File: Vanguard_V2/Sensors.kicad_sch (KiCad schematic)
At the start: 20 parts, among them IC2 MAX-M10S-00B, IC3 ADXL375BCCZ-RL, IC4 ASM330LHHTR, J7 Conn_Coaxial, U4 LPS22HH, U5 LSM303C

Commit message: V2 Board Ready
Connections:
- net +3.3V: now also C24.1, C25.1, C26.1, IC4.5 (VDDIO)
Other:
- moved on the sheet: C21, C22, C23, C24, C27, C28, C29, C30, D3, FB2, IC2, IC3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

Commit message: started layout for V2.1
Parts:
- R11: footprint Capacitor_SMD:C_0402_1005Metric -> Resistor_SMD:R_0402_1005Metric
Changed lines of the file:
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@@
 			)
 		)
-		(property "Footprint" "Capacitor_SMD:C_0402_1005Metric"
+		(property "Footprint" "Resistor_SMD:R_0402_1005Metric"
 			(at 196.85 126.238 90)
 			(effects

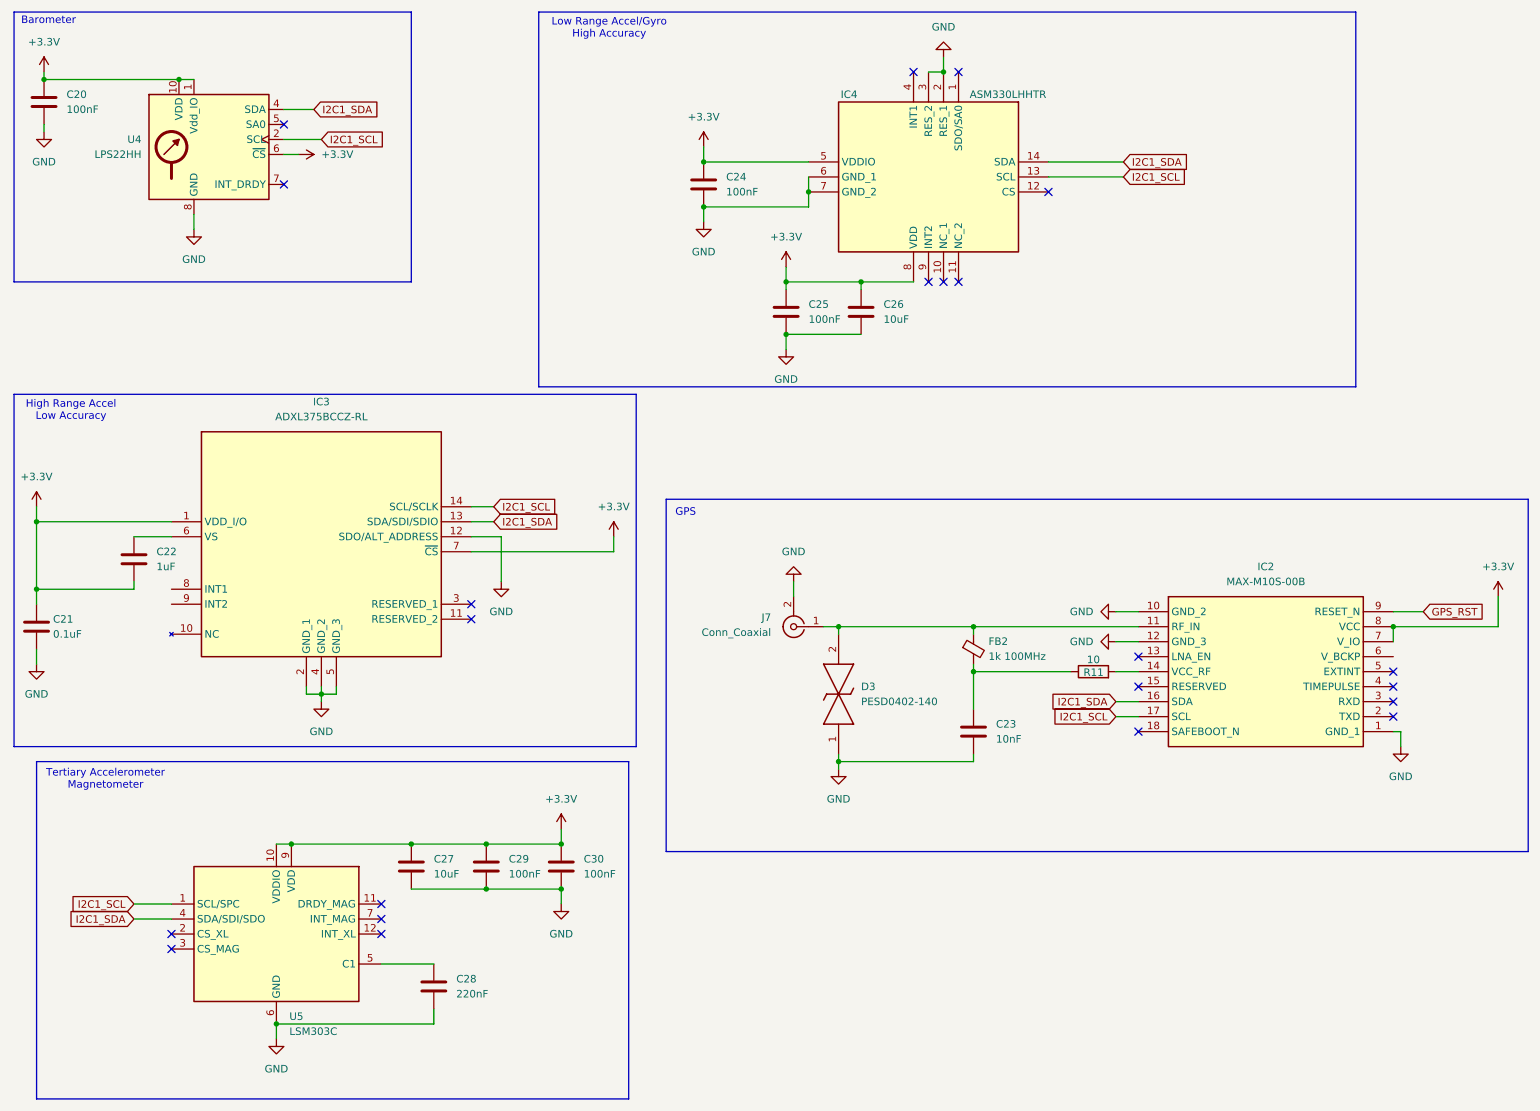
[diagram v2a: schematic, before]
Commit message: Fixed sensors
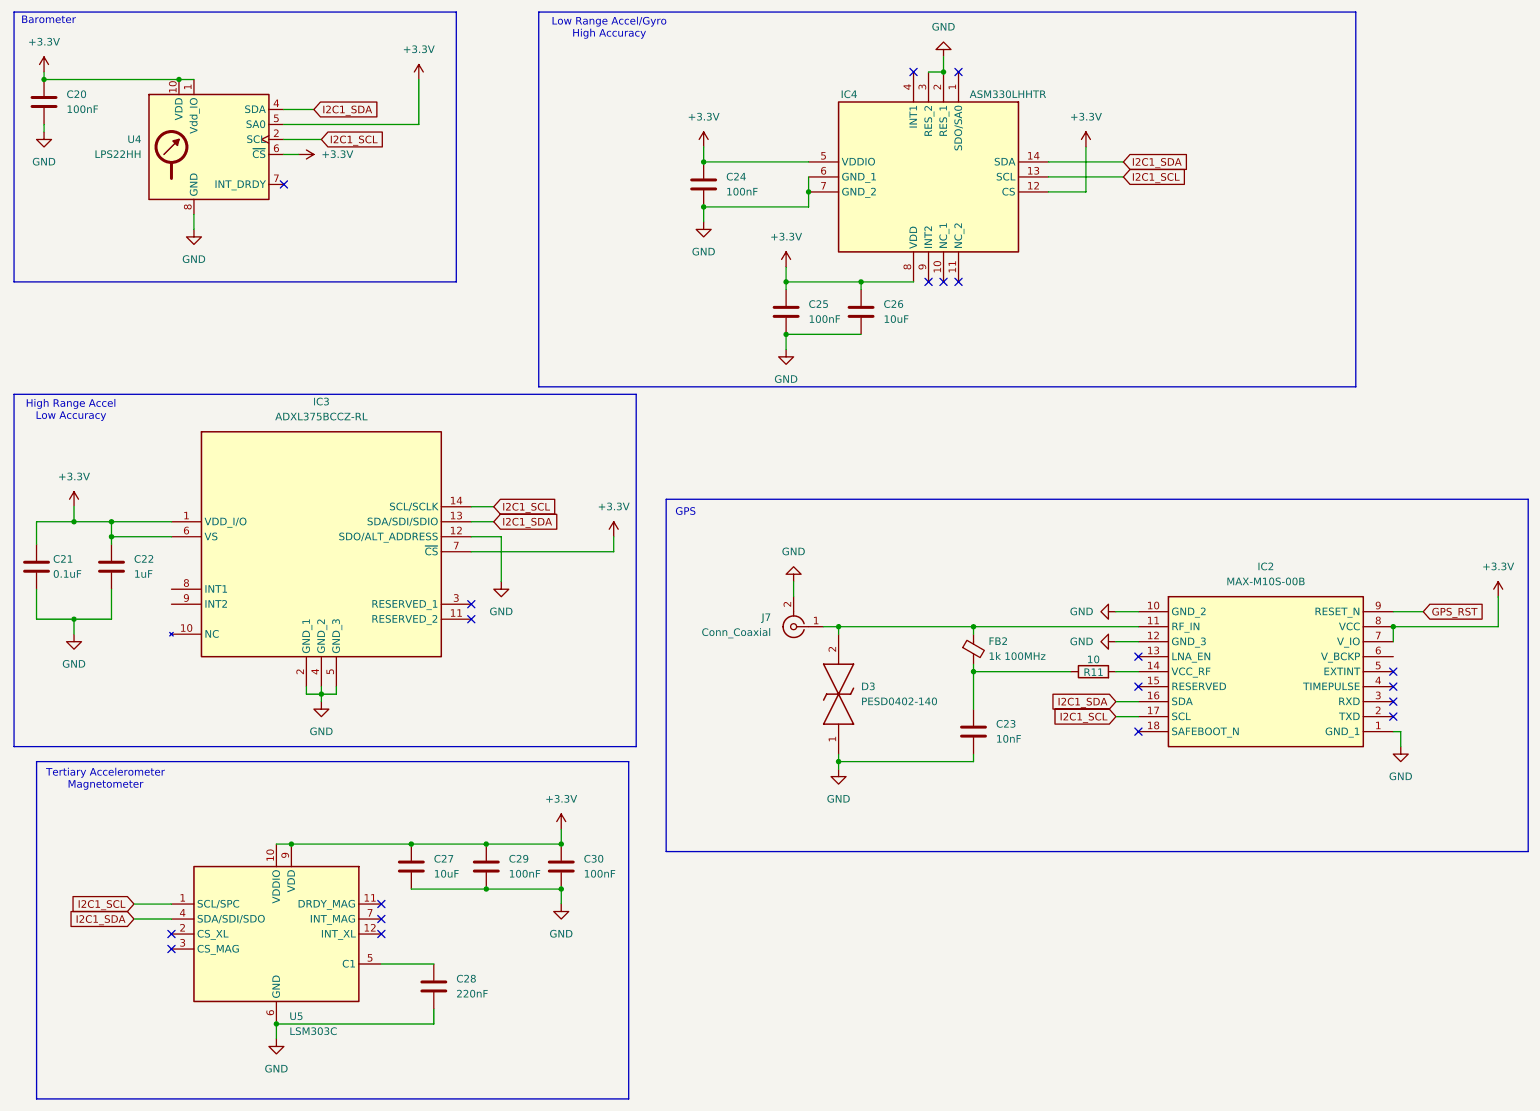
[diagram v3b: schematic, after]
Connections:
- net +3.3V: now also C22.1, IC3.6 (VS), IC4.12 (CS), U4.5 (SA0); no longer C22.2
- net GND: now also C22.2
- no-connect marks 22 -> 20
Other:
- moved on the sheet: C21, C22
